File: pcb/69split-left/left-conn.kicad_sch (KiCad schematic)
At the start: 1 part, among them J1 USB_C_Receptacle

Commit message: Moved things around so it's less confusing.
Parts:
- removed J1: USB_C_Receptacle, Connector_USB:USB_C_Receptacle_Amphenol_12401548E4-2A, symbol Connector:USB_C_Receptacle
- added J3: USB_C_Receptacle, Connector_USB:USB_C_Receptacle_Amphenol_12401548E4-2A, symbol Connector:USB_C_Receptacle
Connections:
- net COL10: now also J3.A3 (TX1-)
- net COL11: now also J3.A2 (TX1+)
- net COL12: now also J3.A10 (RX2-)
- net COL13: now also J3.A11 (RX2+)
- net COL14: now also J3.B3 (TX2-)
- net COL6: now also J3.A6 (D+)
- net COL7: now also J3.B6 (D+)
- net COL8: now also J3.B10 (RX1-)
- net COL9: now also J3.B11 (RX1+)
- net GND: now also J3.A1 (GND), J3.A12 (GND), J3.B1 (GND), J3.B12 (GND), J3.S1 (SHIELD)
- net GPIO_OUT_PB5: now also J3.B8 (SBU2)
- net GPIO_OUT_PB6: now also J3.A8 (SBU1)
- net GPIO_OUT_PB7: now also J3.B2 (TX2+)
- net ROW0: now also J3.A4 (VBUS), J3.A9 (VBUS), J3.B4 (VBUS), J3.B9 (VBUS)
- net ROW1: now also J3.A5 (CC1)
- net ROW2: now also J3.B5 (CC2)
- net ROW3: now also J3.A7 (D-)
- net ROW4: now also J3.B7 (D-)
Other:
- note added: "LEFT KEYBOARD CONNECTOR"
- note removed: "RIGHT KEYBOARD CONNECTOR"

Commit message: Started layout?
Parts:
- J2: renamed from J3; footprint Connector_USB:USB_C_Receptacle_Amphenol_12401548E4-2A -> Connector_USB:USB_C_Receptacle_Amphenol_12401610E4-2A; MPN 12401548E4#2A -> 12401610E4#2A
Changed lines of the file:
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@@
 		(dnp no)
 		(fields_autoplaced yes)
-		(property "Reference" "J3"
+		(property "Reference" "J2"
 			(at 207.01 101.5999 0)
 			(effects
@@
 			)
 		)
-		(property "Footprint" "Connector_USB:USB_C_Receptacle_Amphenol_12401548E4-2A"
+		(property "Footprint" "Connector_USB:USB_C_Receptacle_Amphenol_12401610E4-2A"
 			(at 191.77 99.06 0)
 			(effects
@@
 			)
 		)
-		(property "MPN" "12401548E4#2A "
+		(property "MPN" "12401610E4#2A"
 			(at 195.58 99.06 0)
 			(effects
@@
 			(project "69split-left"
 				(path "/94301c1c-44b1-4926-ac38-8a25b84a2b23/529ccb27-424e-404d-8f7f-2ca17e17c1b0"
-					(reference "J3")
+					(reference "J2")
 					(unit 1)
 				)
@@
 		(dnp no)
 		(fields_autoplaced yes)
-		(property "Reference" "#PWR019"
+		(property "Reference" "#PWR015"
 			(at 199.39 152.4 0)
 			(effects
@@
 			(project "69split-left"
 				(path "/94301c1c-44b1-4926-ac38-8a25b84a2b23/529ccb27-424e-404d-8f7f-2ca17e17c1b0"
-					(reference "#PWR019")
+					(reference "#PWR015")
 					(unit 1)
 				)

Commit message: Continued layout.
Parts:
- J2: footprint Connector_USB:USB_C_Receptacle_Amphenol_12401610E4-2A -> Connector_USB:USB_C_Receptacle_Amphenol_12401548E4-2A; MPN 12401610E4#2A -> 12401548E4#2A
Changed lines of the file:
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@@
 			)
 		)
-		(property "Footprint" "Connector_USB:USB_C_Receptacle_Amphenol_12401610E4-2A"
+		(property "Footprint" "Connector_USB:USB_C_Receptacle_Amphenol_12401548E4-2A"
 			(at 191.77 99.06 0)
 			(effects
@@
 			)
 		)
-		(property "MPN" "12401610E4#2A"
+		(property "MPN" "12401548E4#2A"
 			(at 195.58 99.06 0)
 			(effects

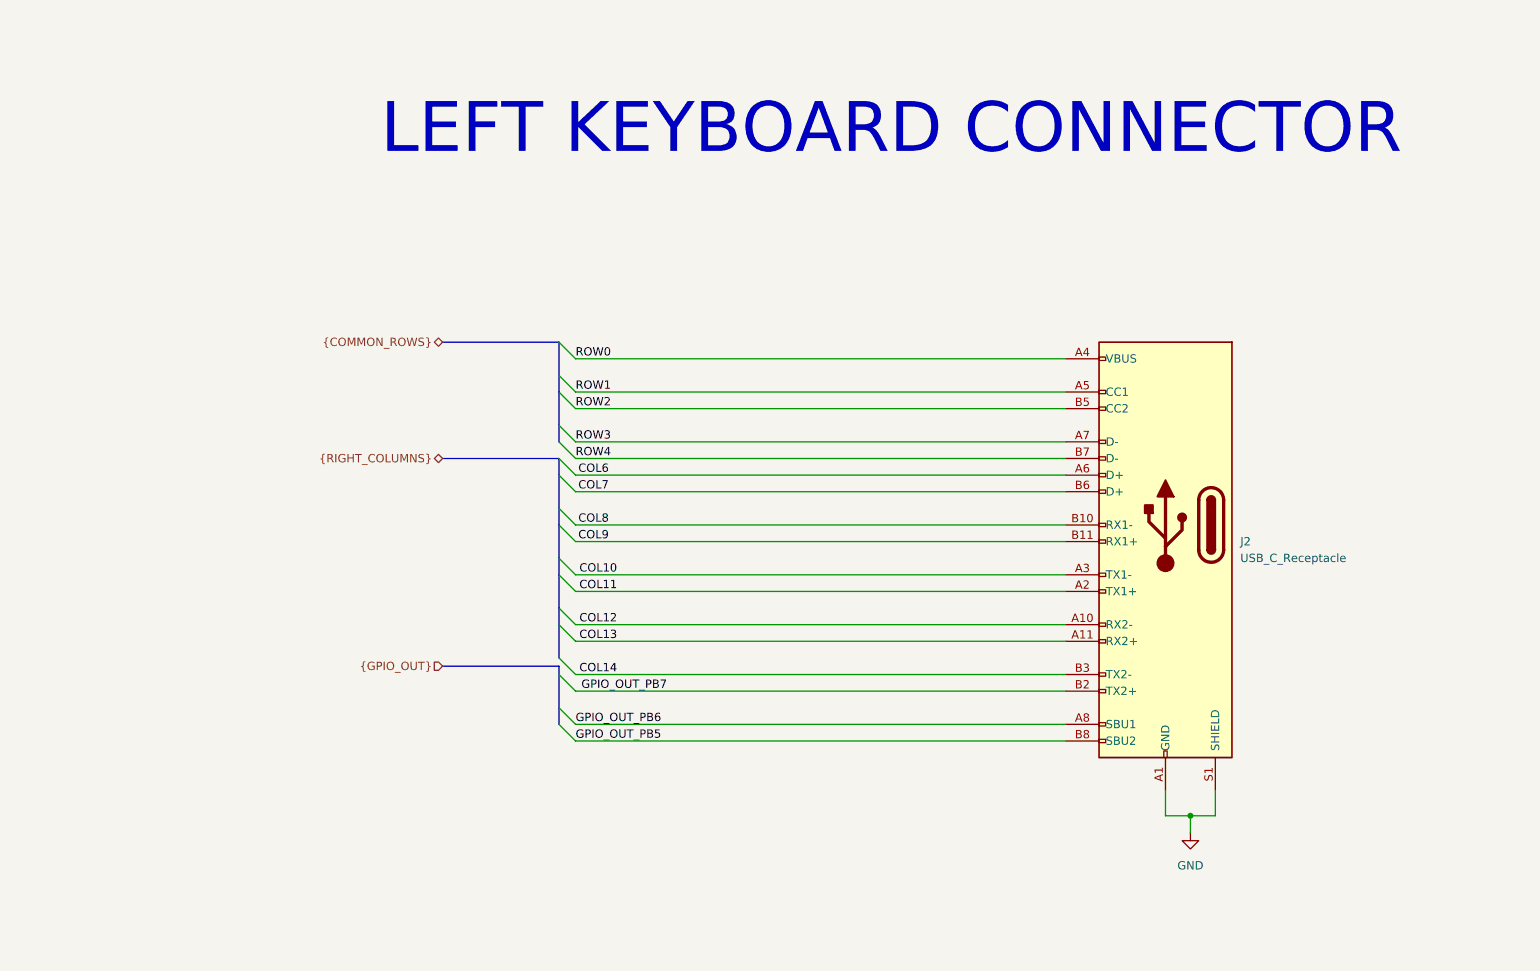
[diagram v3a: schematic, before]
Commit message: Practically finished the left side - need to make a footprint for the split USB connector. Some other schematic changes were made that I will not list. I should've made more commits between ths one and the previous one but it is what it is.
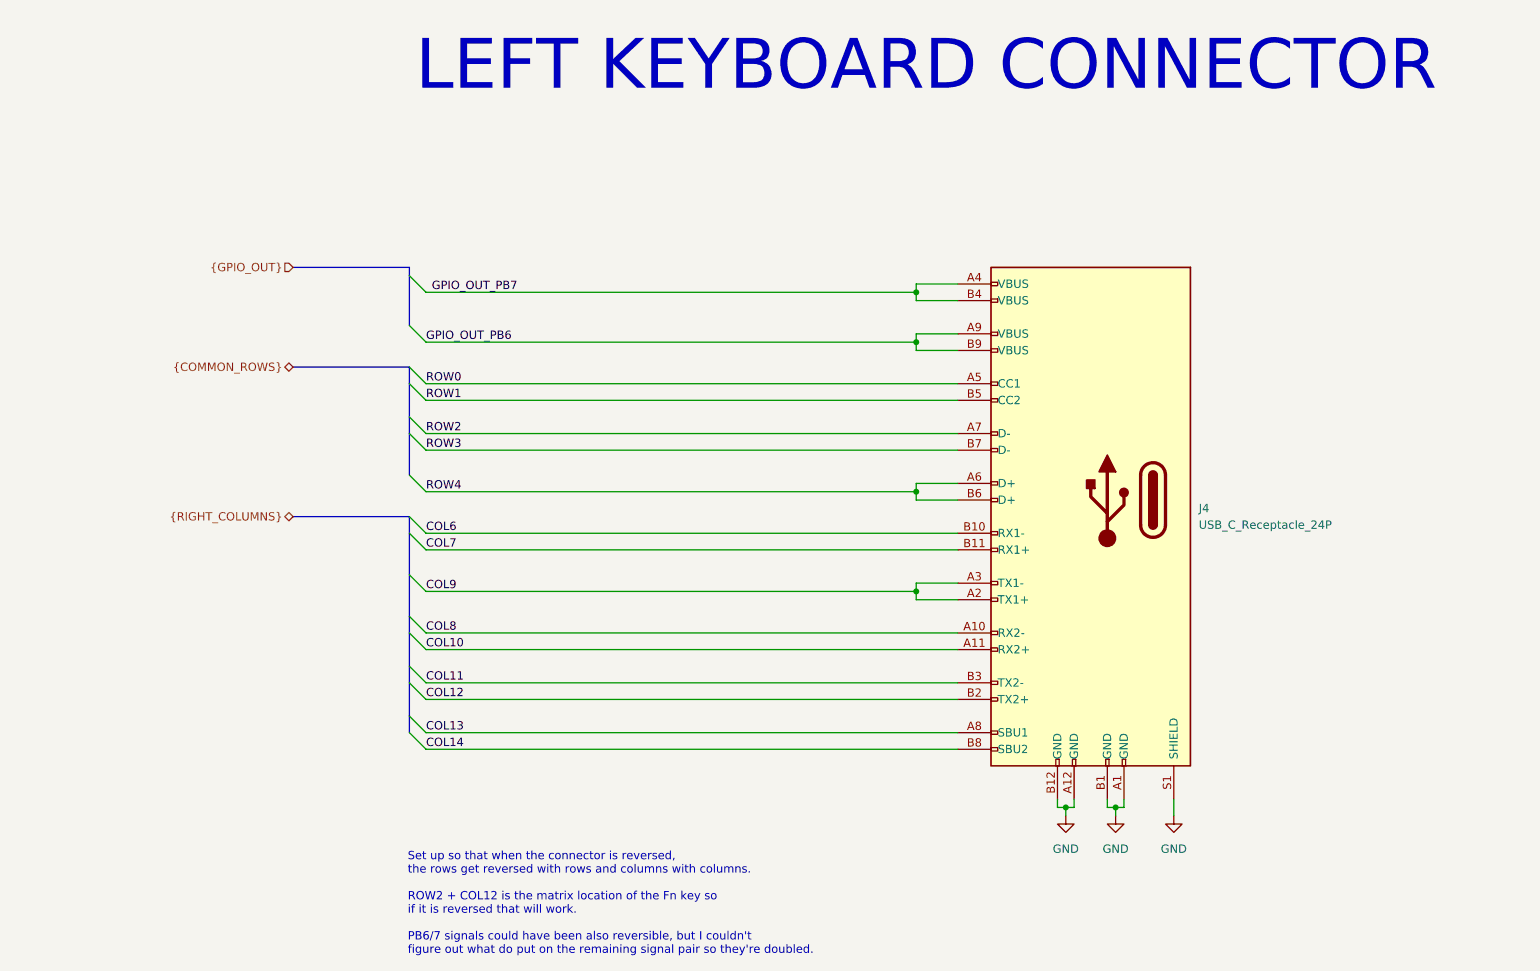
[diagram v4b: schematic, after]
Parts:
- removed J2: USB_C_Receptacle, Connector_USB:USB_C_Receptacle_Amphenol_12401548E4-2A, symbol Connector:USB_C_Receptacle
- added J4: USB_C_Receptacle_24P, symbol Connector:USB_C_Receptacle_24P
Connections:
- net COL10: now also J4.A11 (RX2+)
- net COL11: now also J4.B3 (TX2-)
- net COL12: now also J4.B2 (TX2+)
- net COL13: now also J4.A8 (SBU1)
- net COL14: now also J4.B8 (SBU2)
- net COL6: now also J4.B10 (RX1-)
- net COL7: now also J4.B11 (RX1+)
- net COL8: now also J4.A10 (RX2-)
- net COL9: now also J4.A2 (TX1+), J4.A3 (TX1-)
- net GND: now also J4.A1 (GND), J4.A12 (GND), J4.B1 (GND), J4.B12 (GND), J4.S1 (SHIELD)
- net GPIO_OUT_PB6: now also J4.A9 (VBUS), J4.B9 (VBUS)
- net GPIO_OUT_PB7: now also J4.A4 (VBUS), J4.B4 (VBUS)
- net ROW0: now also J4.A5 (CC1)
- net ROW1: now also J4.B5 (CC2)
- net ROW2: now also J4.A7 (D-)
- net ROW3: now also J4.B7 (D-)
- net ROW4: now also J4.A6 (D+), J4.B6 (D+)
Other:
- note added: "Set up so that when the connector is reversed, the rows get reversed with rows and columns with columns. ROW2 + COL12 is the matrix location of the Fn key so if it is reversed that will work. PB6/7 signals could have been also reversible, but I couldn't figure out what do put on the remaining signal pair so they're doubled."

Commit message: Started changing things gain to use an I/O expander with I2C.
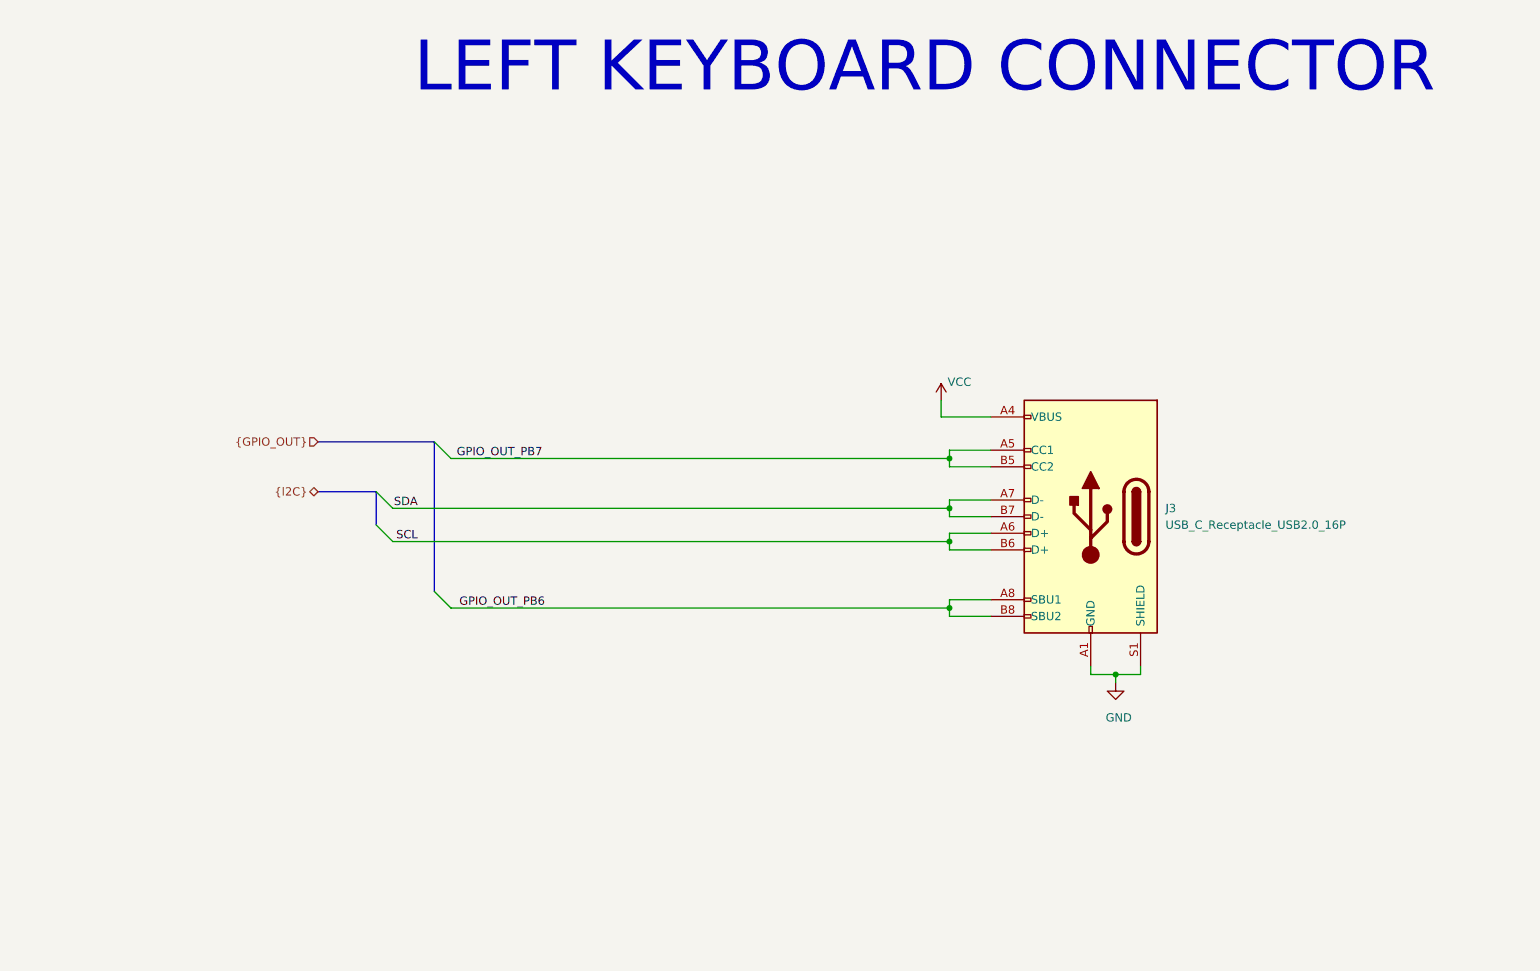
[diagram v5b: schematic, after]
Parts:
- J3: renamed from J4; value USB_C_Receptacle_24P -> USB_C_Receptacle_USB2.0_16P; footprint (none) -> Connector_USB:USB_C_Receptacle_JAE_DX07S016JA1R1500; symbol Connector:USB_C_Receptacle_24P -> Connector:USB_C_Receptacle_USB2.0_16P; MPN (none) -> DX07S016JA1R1500
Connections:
- net COL13 is gone; now on net GPIO_OUT_PB6: J3.A8 (SBU1)
- net COL14 is gone; now on net GPIO_OUT_PB6: J3.B8 (SBU2)
- net ROW0 is gone; now on net GPIO_OUT_PB7: J3.A5 (CC1)
- net ROW1 is gone; now on net GPIO_OUT_PB7: J3.B5 (CC2)
- net ROW3 is gone; now on net SDA: J3.B7 (D-)
- net GPIO_OUT_PB6: no longer J3.A9 (VBUS), J3.B9 (VBUS)
- net GPIO_OUT_PB7: no longer J3.A4 (VBUS), J3.B4 (VBUS)
- removed net COL10: J3.A11 (RX2+)
- removed net COL11: J3.B3 (TX2-)
- removed net COL12: J3.B2 (TX2+)
- removed net COL6: J3.B10 (RX1-)
- removed net COL7: J3.B11 (RX1+)
- removed net COL8: J3.A10 (RX2-)
- removed net COL9: J3.A2 (TX1+), J3.A3 (TX1-)
- net ROW2 renamed SDA
- net ROW4 renamed SCL
- new net VCC: J3.A4 (VBUS), J3.A9 (VBUS), J3.B4 (VBUS), J3.B9 (VBUS)
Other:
- note removed: "Set up so that when the connector is reversed, the rows get reversed with rows and columns with columns. ROW2 + COL12 is the matrix location of the Fn key so if it is reversed that will work. PB6/7 signals could have been also reversible, but I couldn't figure out what do put on the remaining signal pair so they're doubled."
- company: (none) -> Yiannis Michael
- title: 69SPLIT KEYBOARD -> 69SPLIT

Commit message: Final touches.
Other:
- moved on the sheet: J3
